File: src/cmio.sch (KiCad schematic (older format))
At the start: 47 parts, among them J1 USB_POWER, J2 BANK0, J3 USB_OTG, J4 CM3Lite, J5 TVOUT, J7 Micro_SD_Card_TFP09_2_12B, J9 Micro_SD_Card_Molex_47219-2001, Q1 2N7002, Q2 2N7002, SW1 Reset, U1 AP3417B, U2 AP3417B, U3 AP2138, U4 AP2401

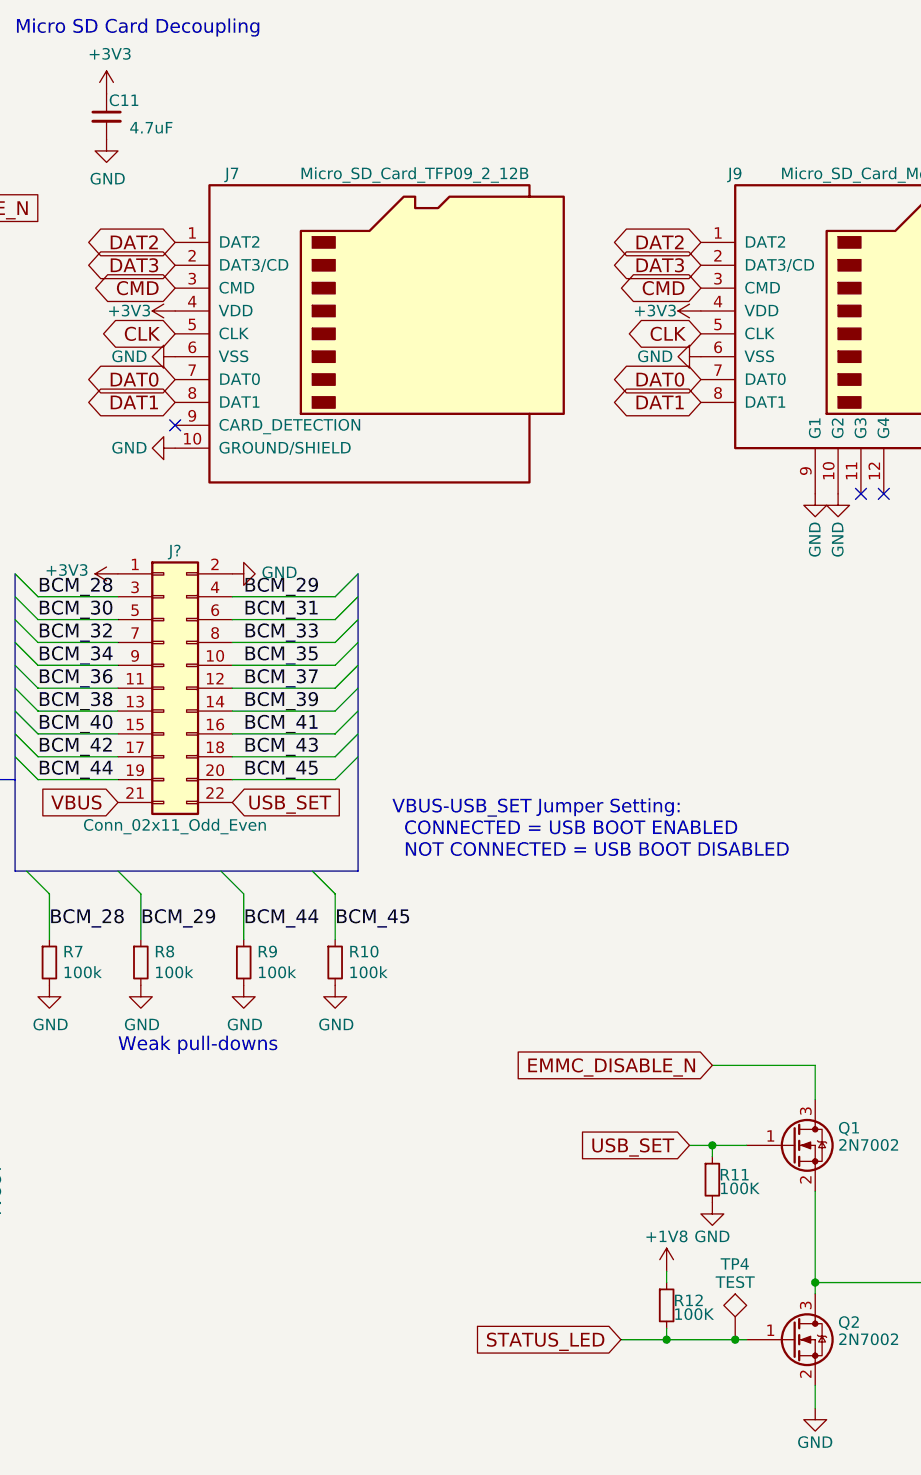
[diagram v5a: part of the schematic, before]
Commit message: Minor changes
These are minor changes that missed previous commits as I forgot to
save.

Signed-off-by: Mahyar Koshkouei <mahyar.koshkouei@gmail.com>
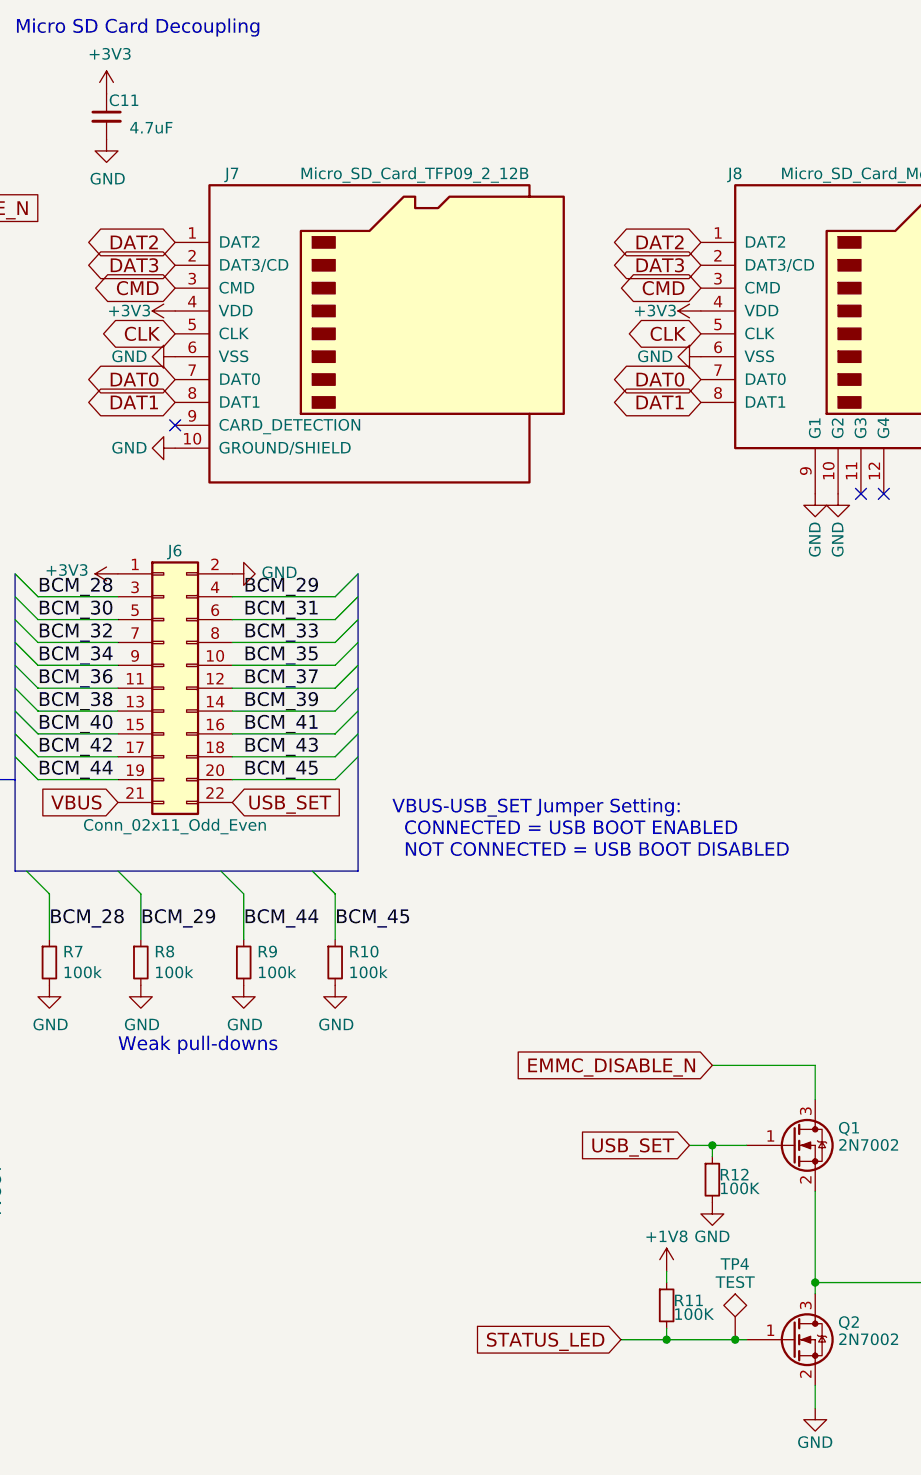
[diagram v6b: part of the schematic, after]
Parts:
- J6: renamed from J?; footprint (none) -> Pin_Headers:Pin_Header_Straight_2x11_Pitch2.54mm_SMD
- renumbered J9 to J8, R12 to R11, R11 to R12
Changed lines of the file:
@@
 $EndComp
 $Comp
-L Micro_SD_Card_Molex_47219-2001 J9
+L Micro_SD_Card_Molex_47219-2001 J8
 U 1 1 5A0695F4
 P 15200 2000
-F 0 "J9" H 14450 2700 50  0000 C CNN
+F 0 "J8" H 14450 2700 50  0000 C CNN
 F 1 "Micro_SD_Card_Molex_47219-2001" H 15850 2700 50  0000 R CNN
 F 2 "foot:Molex_Micro_SD_47309-3751" H 17250 2700 50  0001 C CNN
@@
 $EndComp
 $Comp
-L R_Small R12
+L R_Small R11
 U 1 1 5A087704
 P 14150 6250
-F 0 "R12" H 14180 6270 50  0000 L CNN
+F 0 "R11" H 14180 6270 50  0000 L CNN
 F 1 "100K" H 14180 6210 50  0000 L CNN
 F 2 "Resistors_SMD:R_0805_HandSoldering" H 14150 6250 50  0001 C CNN
@@
 VBUS
 $Comp
-L R_Small R11
+L R_Small R12
 U 1 1 5A0961F7
 P 14350 5700
-F 0 "R11" H 14380 5720 50  0000 L CNN
+F 0 "R12" H 14380 5720 50  0000 L CNN
 F 1 "100K" H 14380 5660 50  0000 L CNN
 F 2 "Resistors_SMD:R_0805_HandSoldering" H 14350 5700 50  0001 C CNN
@@
 VBUS-USB_SET Jumper Setting:\n  CONNECTED = USB BOOT ENABLED\n  NOT CONNECTED = USB BOOT DISABLED
 $Comp
-L Conn_02x11_Odd_Even J?
+L Conn_02x11_Odd_Even J6
 U 1 1 5A09B0DE
 P 11950 3550
-F 0 "J?" H 12000 4150 50  0000 C CNN
+F 0 "J6" H 12000 4150 50  0000 C CNN
 F 1 "Conn_02x11_Odd_Even" H 12000 2950 50  0000 C CNN
-F 2 "" H 11950 3550 50  0001 C CNN
+F 2 "Pin_Headers:Pin_Header_Straight_2x11_Pitch2.54mm_SMD" H 11950 3550 50  0001 C CNN
 F 3 "" H 11950 3550 50  0001 C CNN
 	1    11950 3550

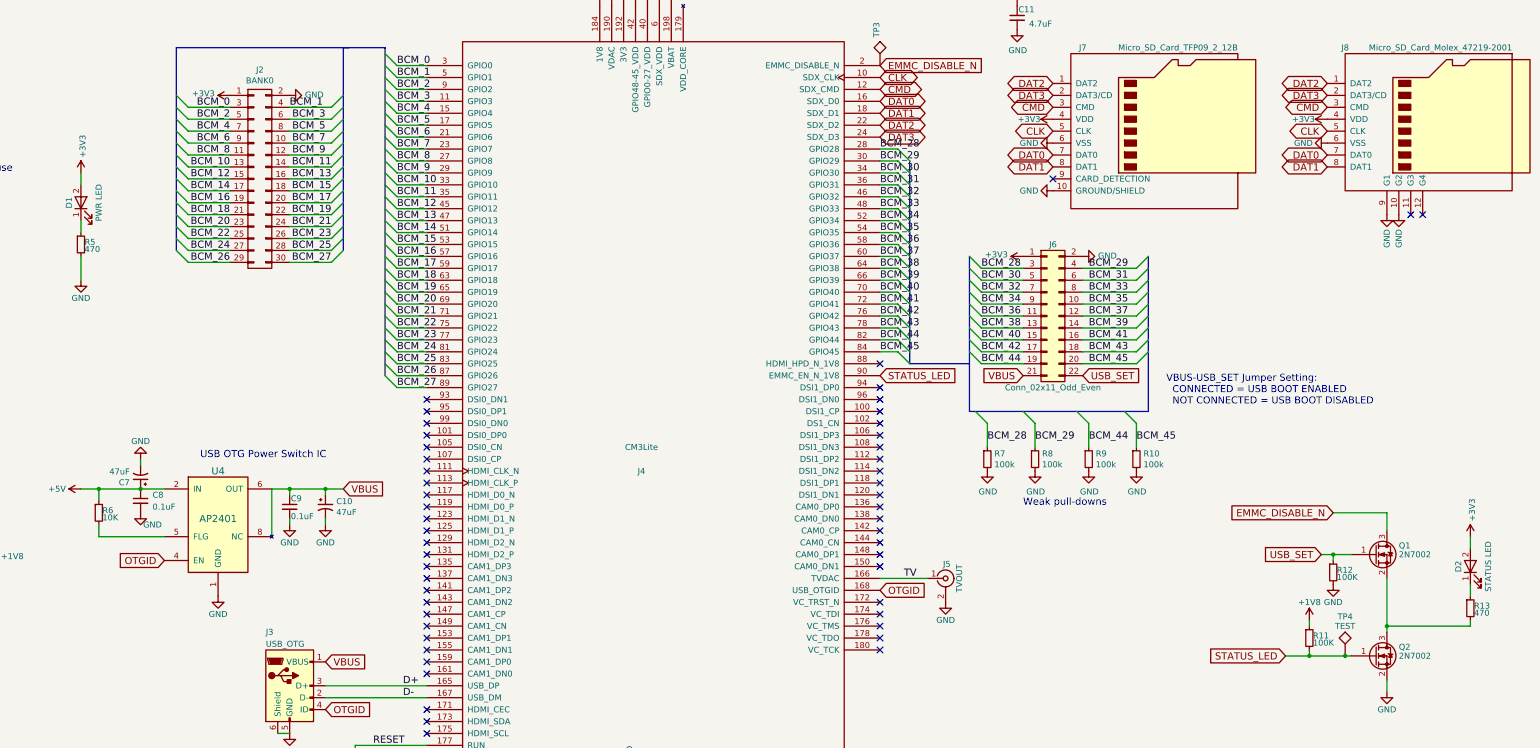
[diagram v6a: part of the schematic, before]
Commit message: Complete Routing
Signed-off-by: Mahyar Koshkouei <mahyar.koshkouei@gmail.com>
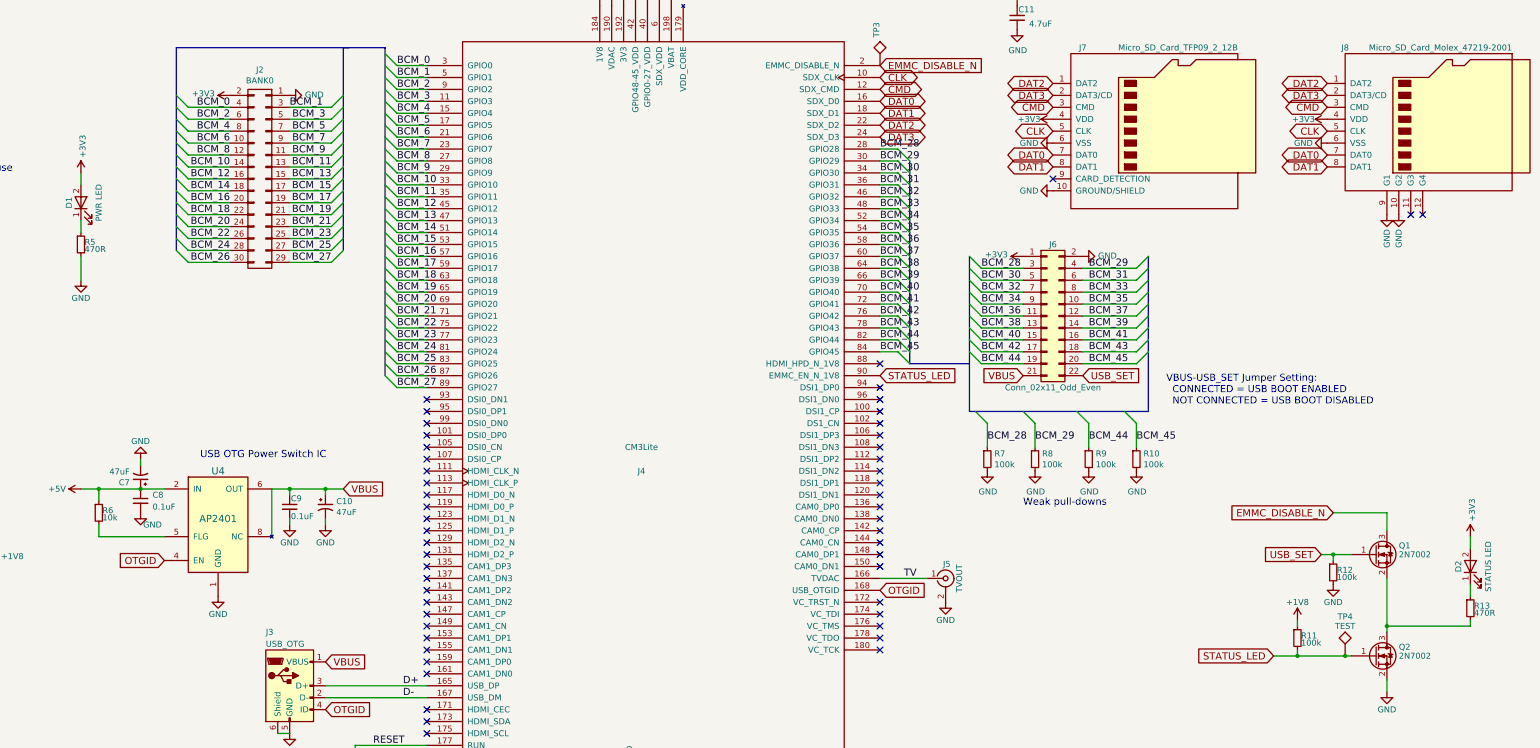
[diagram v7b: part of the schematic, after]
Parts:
- R11, R12: value 100K -> 100k
- R13, R5: value 470 -> 470R
- R6: value 10K -> 10k
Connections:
- net +3V3: now also J2.2 (P2); no longer J2.1 (P1)
- net BCM_0: now also J2.4 (P4); no longer J2.3 (P3)
- net BCM_1: now also J2.3 (P3); no longer J2.4 (P4)
- net BCM_10: now also J2.14 (P14); no longer J2.13 (P13)
- net BCM_11: now also J2.13 (P13); no longer J2.14 (P14)
- net BCM_12: now also J2.16 (P16); no longer J2.15 (P15)
- net BCM_13: now also J2.15 (P15); no longer J2.16 (P16)
- net BCM_14: now also J2.18 (P18); no longer J2.17 (P17)
- net BCM_15: now also J2.17 (P17); no longer J2.18 (P18)
- net BCM_16: now also J2.20 (P20); no longer J2.19 (P19)
- net BCM_17: now also J2.19 (P19); no longer J2.20 (P20)
- net BCM_18: now also J2.22 (P22); no longer J2.21 (P21)
- net BCM_19: now also J2.21 (P21); no longer J2.22 (P22)
- net BCM_2: now also J2.6 (P6); no longer J2.5 (P5)
- net BCM_20: now also J2.24 (P24); no longer J2.23 (P23)
- net BCM_21: now also J2.23 (P23); no longer J2.24 (P24)
- net BCM_22: now also J2.26 (P26); no longer J2.25 (P25)
- net BCM_23: now also J2.25 (P25); no longer J2.26 (P26)
- net BCM_24: now also J2.28 (P28); no longer J2.27 (P27)
- net BCM_25: now also J2.27 (P27); no longer J2.28 (P28)
- net BCM_26: now also J2.30 (P30); no longer J2.29 (P29)
- net BCM_27: now also J2.29 (P29); no longer J2.30 (P30)
- net BCM_3: now also J2.5 (P5); no longer J2.6 (P6)
- net BCM_4: now also J2.8 (P8); no longer J2.7 (P7)
- net BCM_5: now also J2.7 (P7); no longer J2.8 (P8)
- net BCM_6: now also J2.10 (P10); no longer J2.9 (P9)
- net BCM_7: now also J2.9 (P9); no longer J2.10 (P10)
- net BCM_8: now also J2.12 (P12); no longer J2.11 (P11)
- net BCM_9: now also J2.11 (P11); no longer J2.12 (P12)
- net GND: now also J2.1 (P1); no longer J2.2 (P2)
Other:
- moved on the sheet: R11
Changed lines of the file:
@@
 P 4000 5200
 F 0 "R6" H 4030 5220 50  0000 L CNN
-F 1 "10K" H 4030 5160 50  0000 L CNN
+F 1 "10k" H 4030 5160 50  0000 L CNN
 F 2 "Resistors_SMD:R_0805_HandSoldering" H 4000 5200 50  0001 C CNN
 F 3 "" H 4000 5200 50  0001 C CNN
@@
 F 3 "" H 5350 1250 50  0001 C CNN
 	1    5350 2400
-	1    0    0    -1
+	-1   0    0    -1
 $EndComp
 Entry Wire Line
@@
 P 15500 6000
 F 0 "R13" H 15530 6020 50  0000 L CNN
-F 1 "470" H 15530 5960 50  0000 L CNN
+F 1 "470R" H 15530 5960 50  0000 L CNN
 F 2 "Resistors_SMD:R_0805_HandSoldering" H 15500 6000 50  0001 C CNN
 F 3 "" H 15500 6000 50  0001 C CNN
@@
 	1    0    0    -1
 $EndComp
-Text GLabel 13950 6400 0    60   Input ~ 0
+Text GLabel 13850 6400 0    60   Input ~ 0
 STATUS_LED
 Text GLabel 10550 4050 2    60   Input ~ 0
@@
 P 3850 2950
 F 0 "R5" H 3880 2970 50  0000 L CNN
-F 1 "470" H 3880 2910 50  0000 L CNN
+F 1 "470R" H 3880 2910 50  0000 L CNN
 F 2 "Resistors_SMD:R_0805_HandSoldering" H 3850 2950 50  0001 C CNN
 F 3 "" H 3850 2950 50  0001 C CNN
@@
 L R_Small R11
 U 1 1 5A087704
-P 14150 6250
-F 0 "R11" H 14180 6270 50  0000 L CNN
-F 1 "100K" H 14180 6210 50  0000 L CNN
-F 2 "Resistors_SMD:R_0805_HandSoldering" H 14150 6250 50  0001 C CNN
-F 3 "" H 14150 6250 50  0001 C CNN
-	1    14150 6250
+P 14050 6250
+F 0 "R11" H 14080 6270 50  0000 L CNN
+F 1 "100k" H 14080 6210 50  0000 L CNN
+F 2 "Resistors_SMD:R_0805_HandSoldering" H 14050 6250 50  0001 C CNN
+F 3 "" H 14050 6250 50  0001 C CNN
+	1    14050 6250
 	1    0    0    -1
 $EndComp
@@
 L +1V8 #PWR059
 U 1 1 5A0891B6
-P 14150 6100
-F 0 "#PWR059" H 14150 5950 50  0001 C CNN
-F 1 "+1V8" H 14150 6250 50  0000 C CNN
-F 2 "" H 14150 6100 50  0001 C CNN
-F 3 "" H 14150 6100 50  0001 C CNN
-	1    14150 6100
+P 14050 6100
+F 0 "#PWR059" H 14050 5950 50  0001 C CNN
+F 1 "+1V8" H 14050 6250 50  0000 C CNN
+F 2 "" H 14050 6100 50  0001 C CNN
+F 3 "" H 14050 6100 50  0001 C CNN
+	1    14050 6100
 	1    0    0    -1
 $EndComp
@@
 P 14350 5700
 F 0 "R12" H 14380 5720 50  0000 L CNN
-F 1 "100K" H 14380 5660 50  0000 L CNN
+F 1 "100k" H 14380 5660 50  0000 L CNN
 F 2 "Resistors_SMD:R_0805_HandSoldering" H 14350 5700 50  0001 C CNN
 F 3 "" H 14350 5700 50  0001 C CNN
@@
 	14800 6600 14800 6700
 Wire Wire Line
-	13950 6400 14500 6400
+	13850 6400 14500 6400
 Connection ~ 14450 6400
 Wire Wire Line
@@
 Connection ~ 2150 9000
 Wire Wire Line
-	14150 6350 14150 6400
-Connection ~ 14150 6400
-Wire Wire Line
-	14150 6100 14150 6150
+	14050 6350 14050 6400
+Connection ~ 14050 6400
+Wire Wire Line
+	14050 6100 14050 6150
 Wire Wire Line
 	15500 6150 15500 6100
